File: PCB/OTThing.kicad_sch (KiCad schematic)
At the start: 63 parts, among them IC1 TPS61041, J3 USB_C_Receptacle_USB2.0, Q13 BC847C, SW1 RST/CONFIG, SW2 BOOT, U1 ESP32-C3-WROOM-02, U5 USBLC6-2SC6, U6 AMS1117-3.3

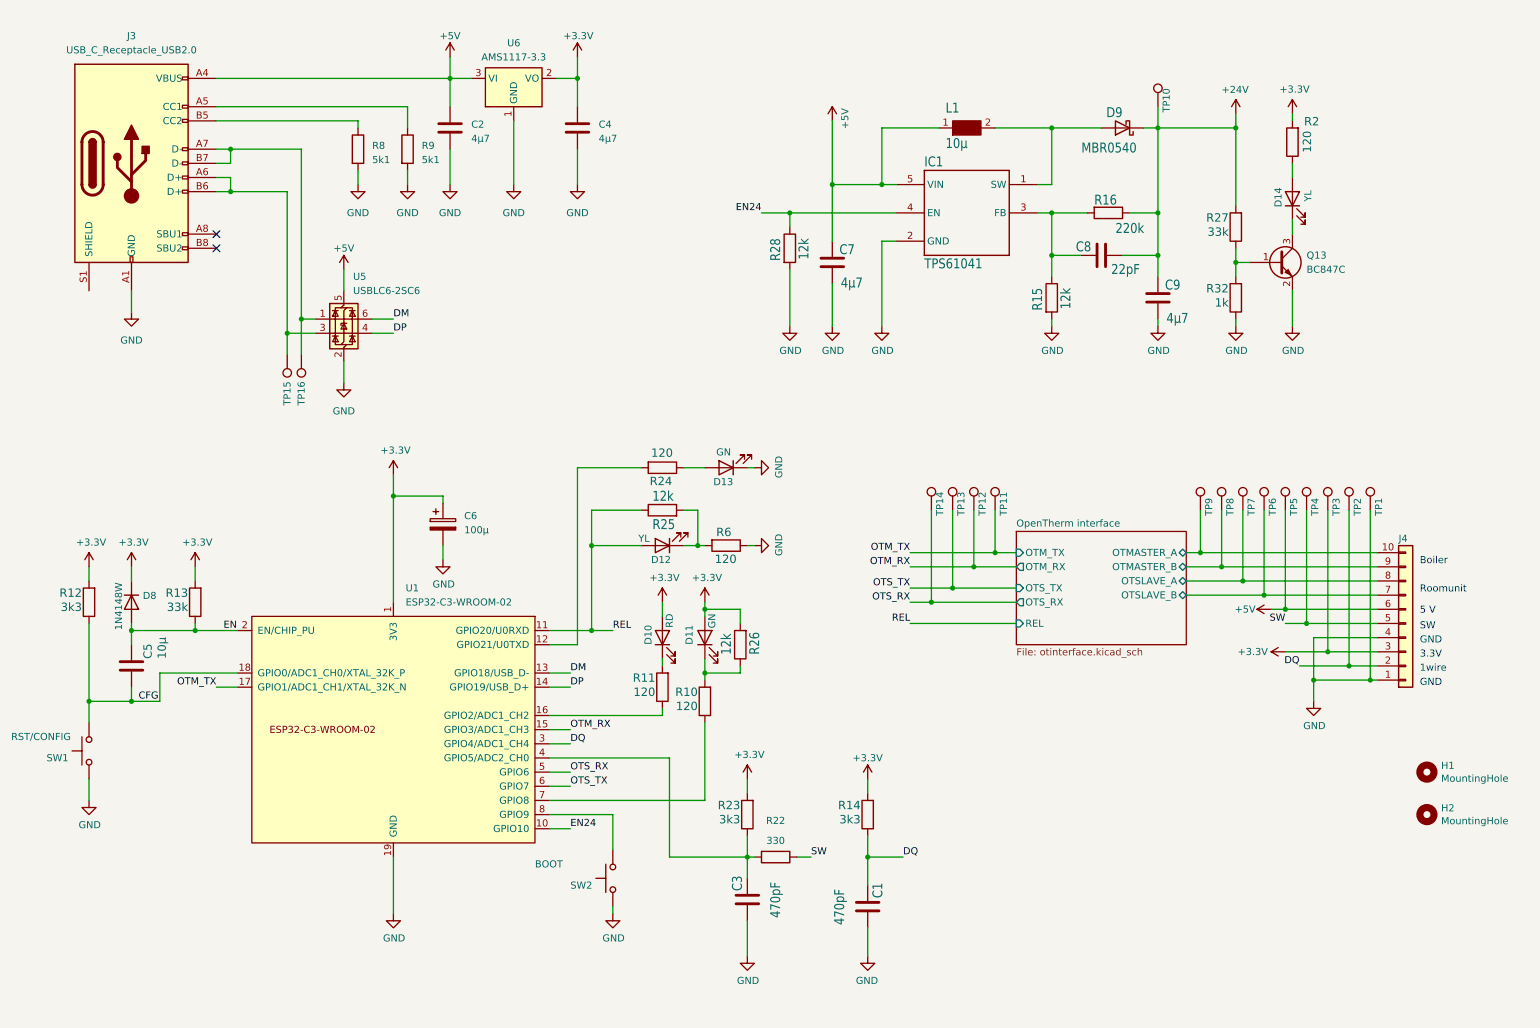
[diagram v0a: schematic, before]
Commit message: Fix ERCs, DRCs & BOM
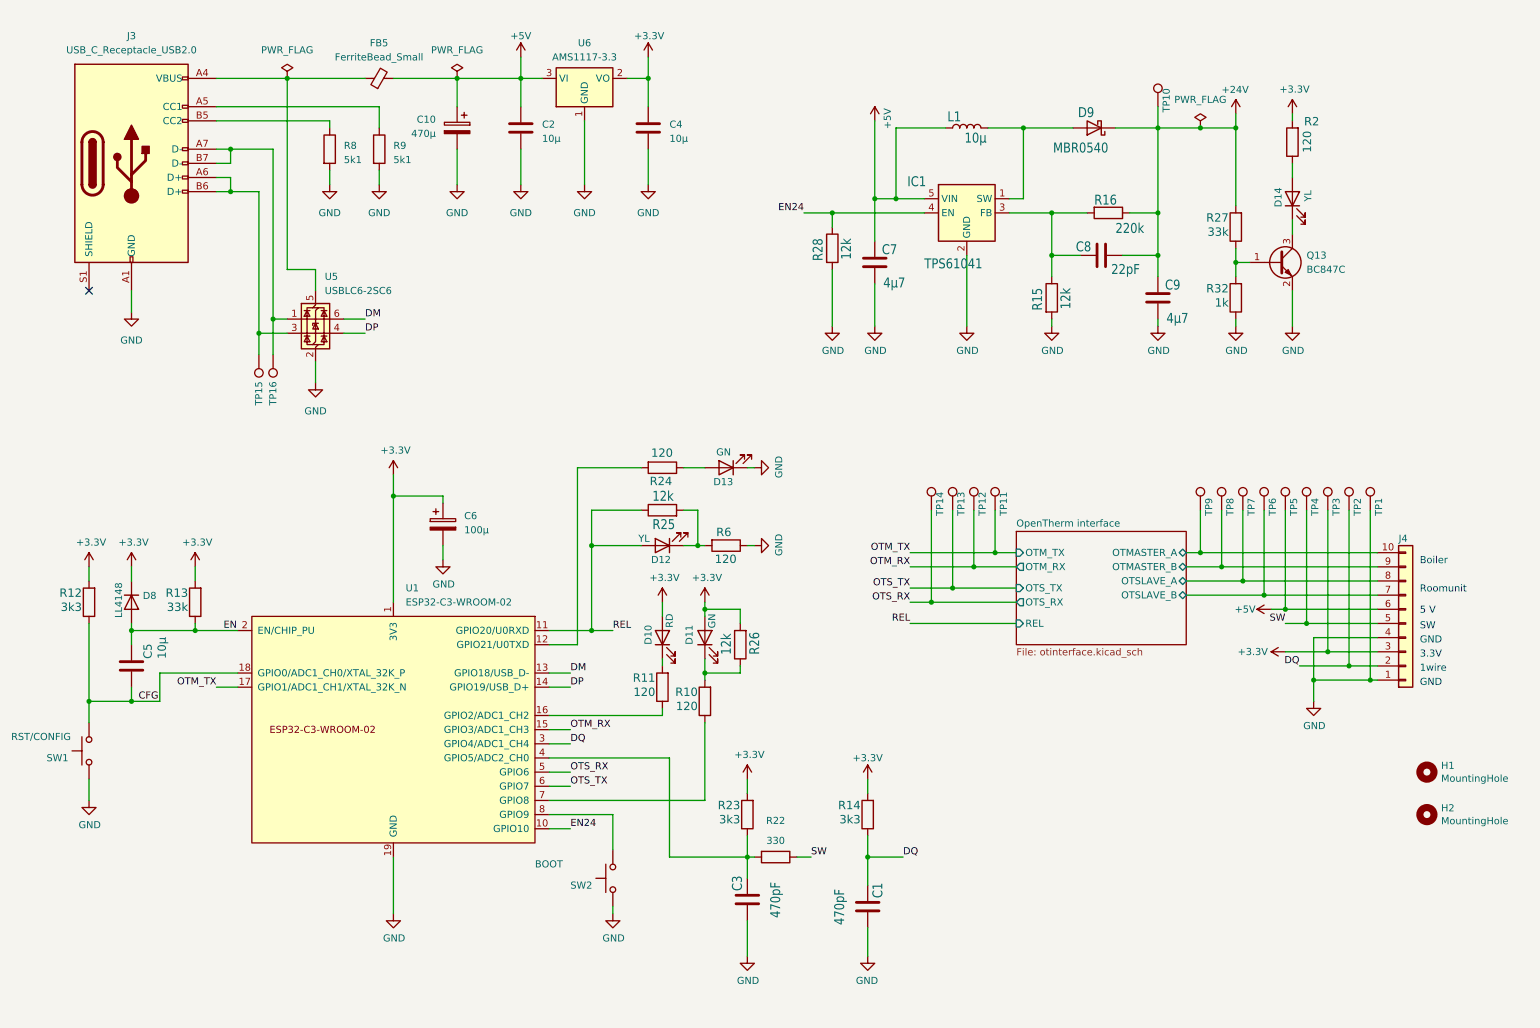
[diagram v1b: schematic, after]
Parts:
- added C10: 470µ, Capacitor_SMD:CP_Elec_6.3x7.7, symbol Device:C_Polarized
- added FB5: FerriteBead_Small, Inductor_SMD:L_0603_1608Metric, symbol Device:FerriteBead_Small
- C2, C4: value 4µ7 -> 10µ; LCSC C2918489 -> C90543
- D8: value 1N4148W -> LL4148; footprint Diode_SMD:D_SOD-123 -> Diode_SMD:D_MiniMELF; LCSC (none) -> C435829
- IC1: footprint Package_TO_SOT_SMD:SOT-23-5_HandSoldering -> Package_TO_SOT_SMD:SOT-23-5; symbol minirx_v4-eagle-import:TPS61040 -> Regulator_Switching:TPS61041DBV
- J3: symbol Connector:USB_C_Receptacle_USB2.0 -> Connector:USB_C_Receptacle_USB2.0_14P
- L1: symbol minirx_v4-eagle-import:WE-PMI_1008 -> Device:L
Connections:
- net +5V: now also C10.1, FB5.2; no longer J3.A4 (VBUS), J3.A9 (VBUS), J3.B4 (VBUS), J3.B9 (VBUS), U5.5 (VBUS)
- net GND: now also C10.2
- new net: FB5.1, J3.A4 (VBUS), J3.A9 (VBUS), J3.B4 (VBUS), J3.B9 (VBUS), U5.5 (VBUS)
- no-connect marks 2 -> 1
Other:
- moved on the sheet: C2, C4, C7, D9, L1, R28, R8, R9, TP15, TP16, U5, U6

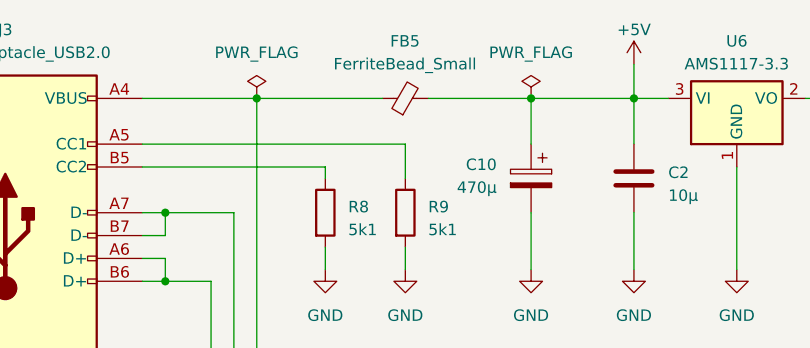
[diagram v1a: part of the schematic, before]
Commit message: update libraries, fix DRCs
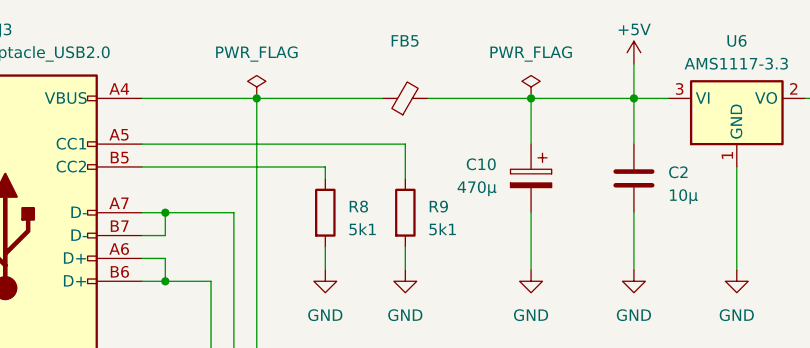
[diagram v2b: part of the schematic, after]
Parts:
- FB5: value FerriteBead_Small -> ~
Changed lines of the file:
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@@
 			)
 		)
-		(property "Value" "FerriteBead_Small"
+		(property "Value" "~"
 			(at 78.7019 25.4 90)
 			(effects
@@
 					(size 1.27 1.27)
 				)
+				(hide yes)
 			)
 		)

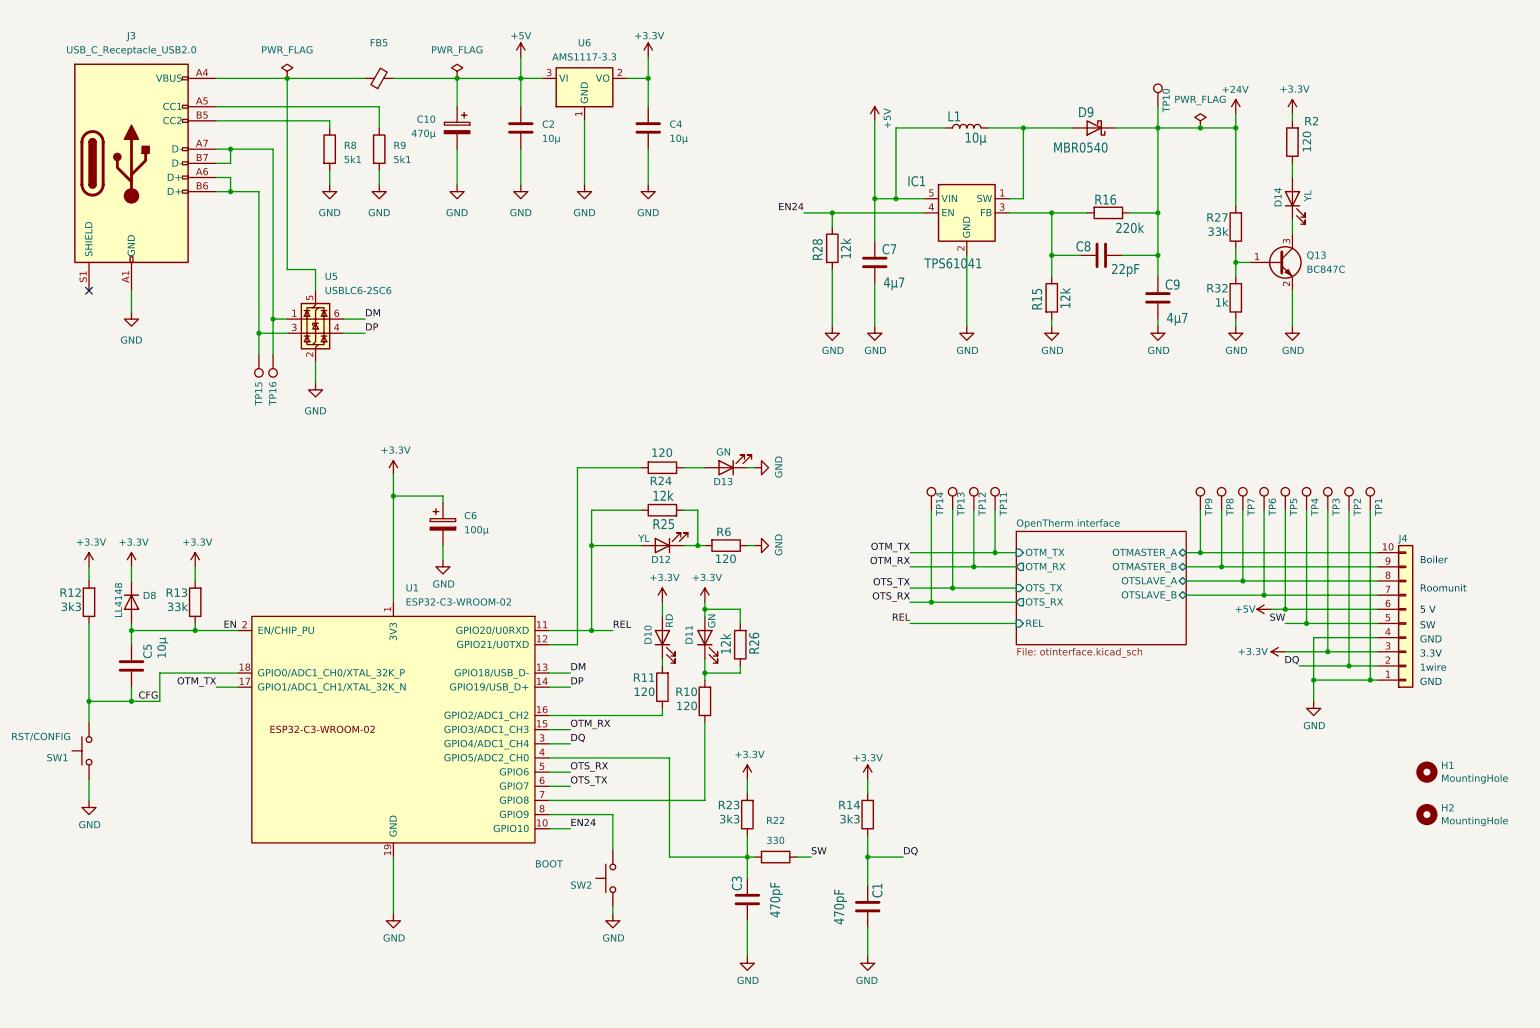
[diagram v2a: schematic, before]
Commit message: sensors for flame / pausetime per cycle aux input sensor
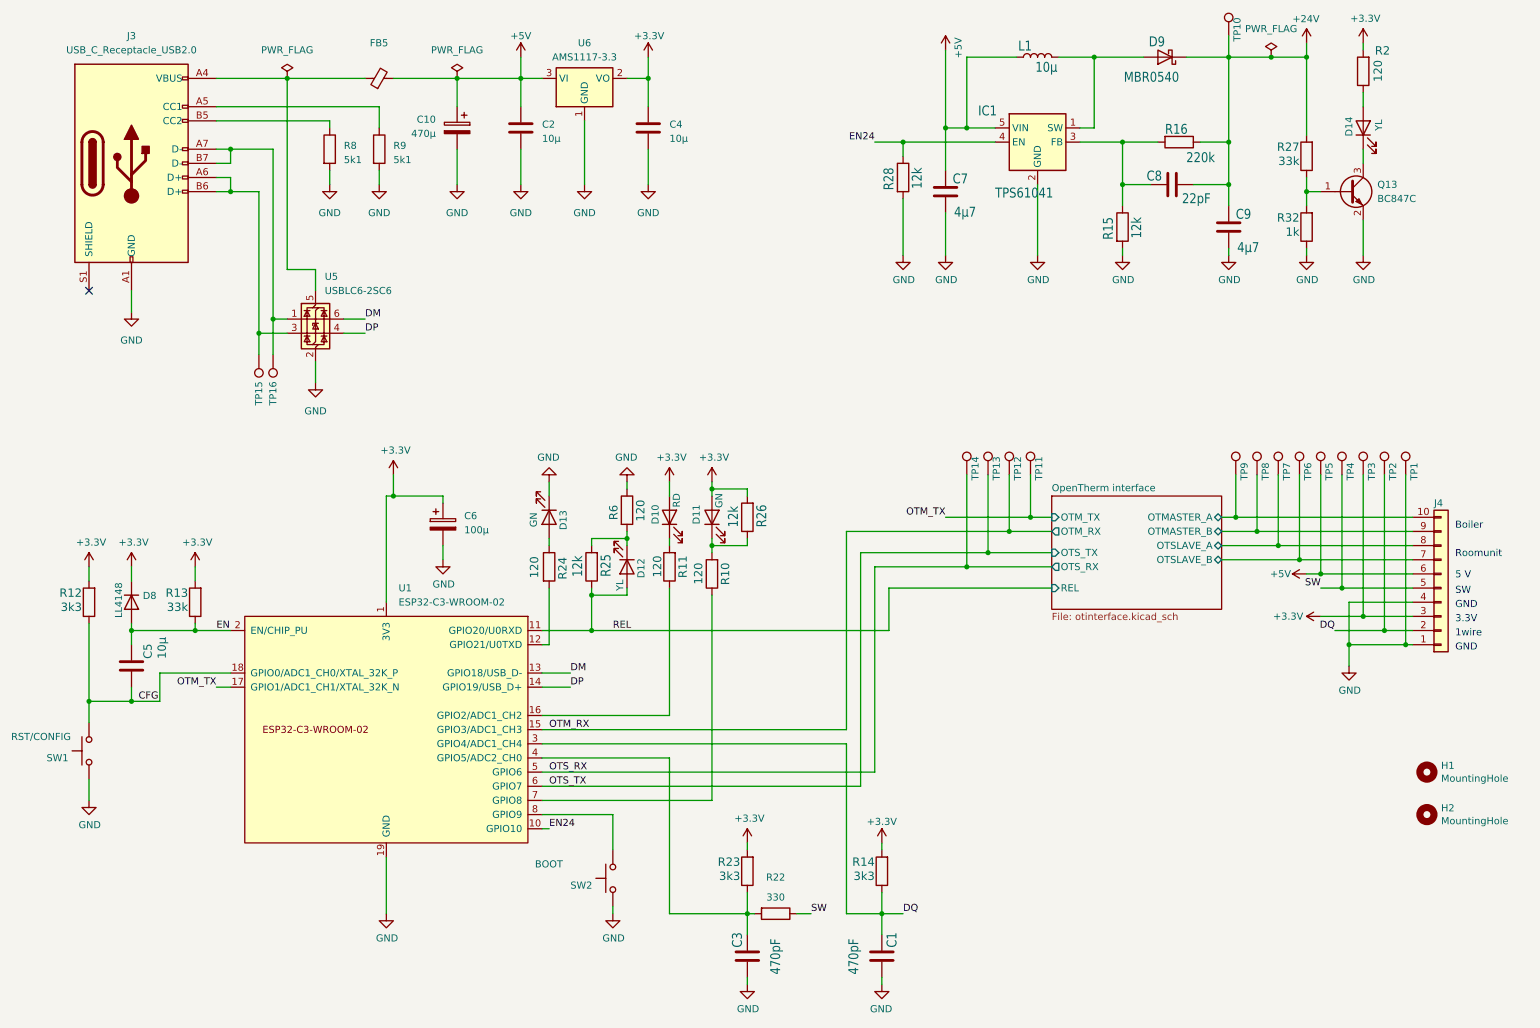
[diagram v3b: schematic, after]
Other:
- moved on the sheet: C1, C3, C7, C8, C9, D10, D11, D12, D13, D14, D9, IC1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

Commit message: fix ERCs & DRCs add TVS diodes to DQ & DI
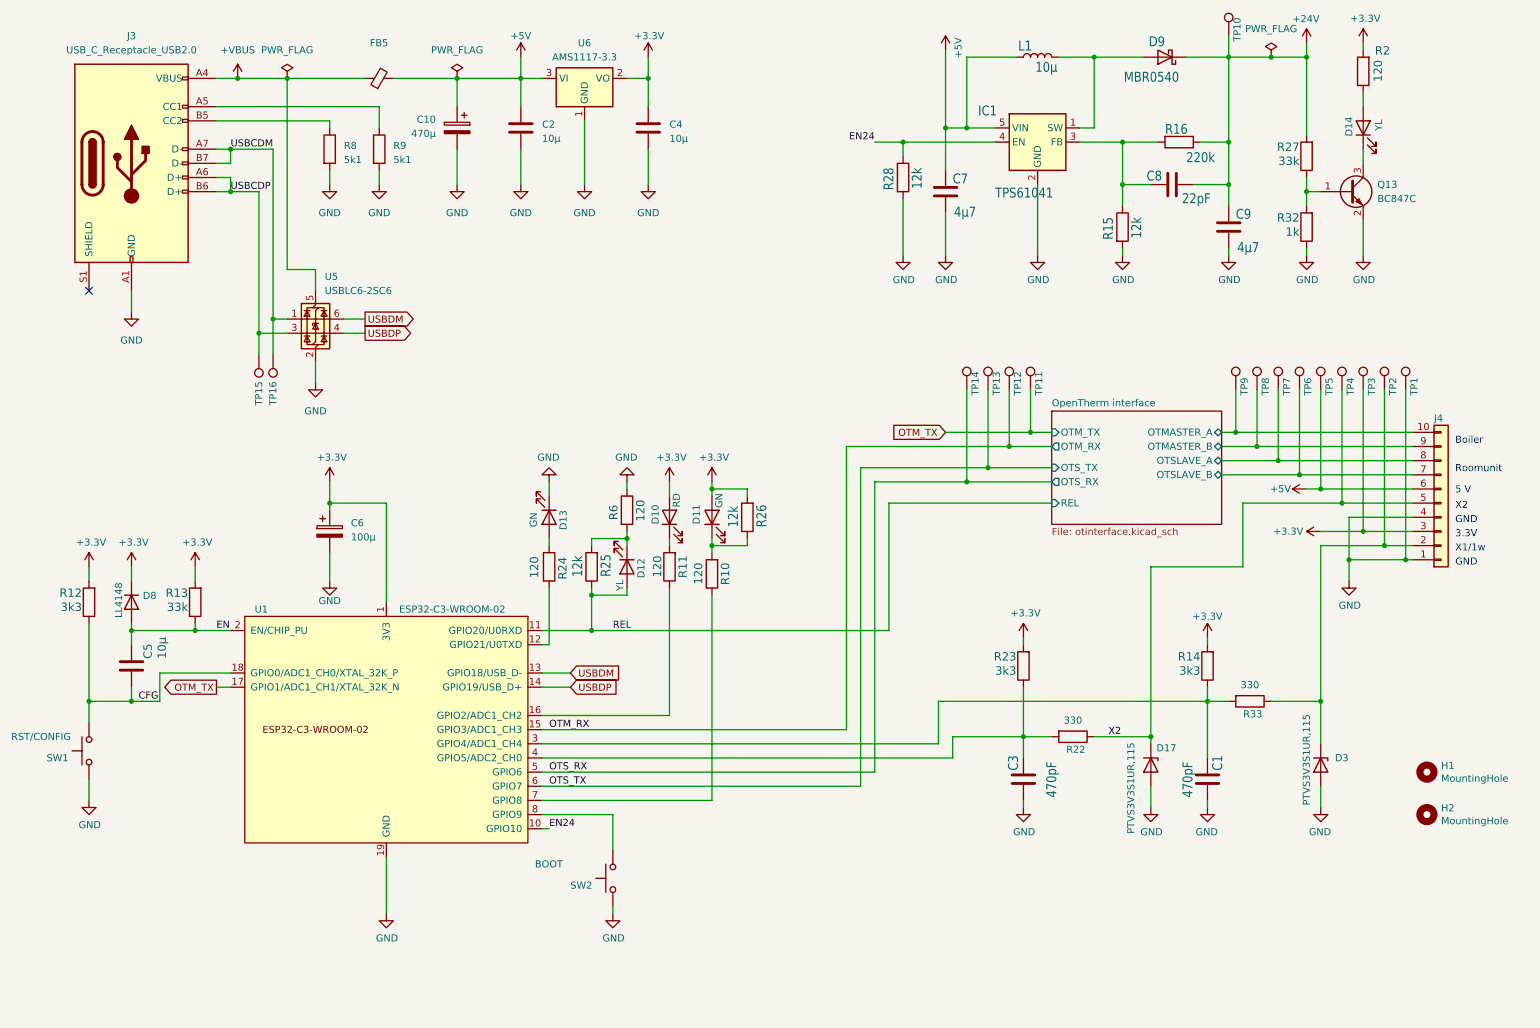
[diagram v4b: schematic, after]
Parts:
- added D17, D3: PTVS3V3S1UR,115, Diode_SMD:D_SOD-123, symbol Device:D_Zener
- added R33: 330, Resistor_SMD:R_0805_2012Metric, symbol Device:R
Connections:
- net GND: now also D17.2 (A), D3.2 (A)
- net USBCDP: now reaches J3.A6 (D+), J3.B6 (D+), TP15.1, U5.3 (I/O2)
- net USBCDM: now reaches J3.A7 (D-), J3.B7 (D-), TP16.1, U5.1 (I/O1)
- net +VBUS: now reaches FB5.1, J3.A4 (VBUS), J3.A9 (VBUS), J3.B4 (VBUS), J3.B9 (VBUS), U5.5 (VBUS)
- net DM renamed USBDM
- net DP renamed USBDP
- net DQ: no longer names the net of C1.1, R14.1, U1.3 (GPIO4/ADC1_CH4)
- net DQ: now also R33.2; no longer J4.2 (Pin_2), TP2.1
- net SW renamed X2
- net X2: now also D17.1 (K)
- new net: D3.1 (K), J4.2 (Pin_2), R33.1, TP2.1
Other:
- note added: "X1/1w"
- note added: "X2"
- note removed: "1wire"
- note removed: "SW"
- moved on the sheet: C1, C3, C6, J4, R14, R22, R23, TP1, TP11, TP12, TP13, TP14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
